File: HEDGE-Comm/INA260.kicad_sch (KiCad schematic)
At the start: 4 parts, among them U6 INA260

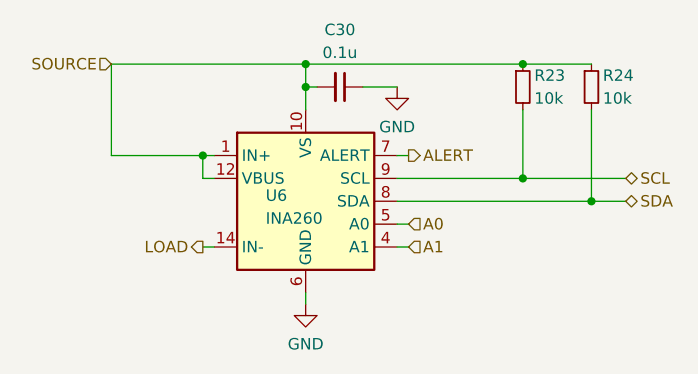
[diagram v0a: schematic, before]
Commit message: Refactor Data PCB files; enter RS485; enter Iridium radio power
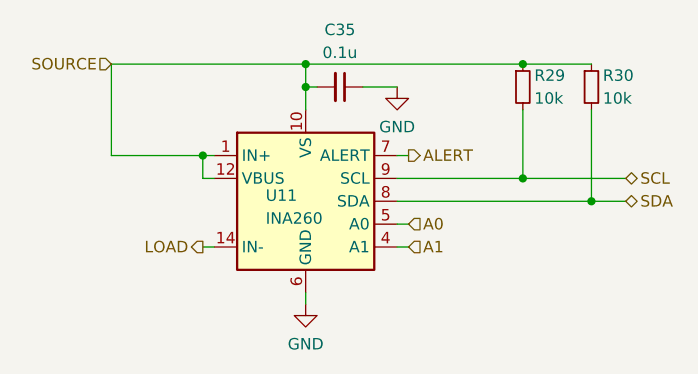
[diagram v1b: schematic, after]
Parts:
- renumbered C30 to C35, R23 to R29, R24 to R30, U6 to U11
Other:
- title: HEDGE-Data PCB -> HEDGE Comm PCB
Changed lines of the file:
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@@
 	(paper "C")
 	(title_block
-		(title "HEDGE-Data PCB")
-		(date "2024-10-09")
+		(title "HEDGE Comm PCB")
+		(date "2024-10-11")
 		(rev "1.0")
 		(company "Spacecraft Design Lab")
@@
 		(on_board yes)
 		(dnp no)
-		(property "Reference" "U6"
+		(property "Reference" "U11"
 			(at 276.225 211.455 0)
 			(effects
@@
 		)
 		(instances
-			(project "HEDGE-Data"
-				(path "/02a0bd66-ef06-41e3-be4b-cca89913b2e5/239e3f0e-d101-4327-8c6c-1d7f43f9fa83"
-					(reference "U6")
-					(unit 1)
-				)
-				(path "/02a0bd66-ef06-41e3-be4b-cca89913b2e5/3d8b74a1-ff69-40df-90d3-fa5176499046"
-					(reference "U7")
-					(unit 1)
-				)
-				(path "/02a0bd66-ef06-41e3-be4b-cca89913b2e5/40d2e298-2505-4869-b40b-0e03f2c17fb7"
-					(reference "U8")
+			(project "Comm"
+				(path "/02a0bd66-ef06-41e3-be4b-cca89913b2e5/98516715-195b-4218-bcff-d5194ed70cb8"
+					(reference "U11")
 					(unit 1)
 				)
@@
 		(dnp no)
 		(fields_autoplaced yes)
-		(property "Reference" "C30"
+		(property "Reference" "C35"
 			(at 284.4736 193.04 90)
 			(effects
@@
 		)
 		(instances
-			(project "HEDGE-Data"
-				(path "/02a0bd66-ef06-41e3-be4b-cca89913b2e5/239e3f0e-d101-4327-8c6c-1d7f43f9fa83"
-					(reference "C30")
-					(unit 1)
-				)
-				(path "/02a0bd66-ef06-41e3-be4b-cca89913b2e5/3d8b74a1-ff69-40df-90d3-fa5176499046"
-					(reference "C31")
-					(unit 1)
-				)
-				(path "/02a0bd66-ef06-41e3-be4b-cca89913b2e5/40d2e298-2505-4869-b40b-0e03f2c17fb7"
-					(reference "C32")
+			(project "Comm"
+				(path "/02a0bd66-ef06-41e3-be4b-cca89913b2e5/98516715-195b-4218-bcff-d5194ed70cb8"
+					(reference "C35")
 					(unit 1)
 				)
@@
 		(on_board yes)
 		(dnp no)
-		(property "Reference" "R24"
+		(property "Reference" "R30"
 			(at 313.69 198.12 0)
 			(effects
@@
 		)
 		(instances
-			(project "HEDGE-Data"
-				(path "/02a0bd66-ef06-41e3-be4b-cca89913b2e5/239e3f0e-d101-4327-8c6c-1d7f43f9fa83"
-					(reference "R24")
-					(unit 1)
-				)
-				(path "/02a0bd66-ef06-41e3-be4b-cca89913b2e5/3d8b74a1-ff69-40df-90d3-fa5176499046"
-					(reference "R26")
-					(unit 1)
-				)
-				(path "/02a0bd66-ef06-41e3-be4b-cca89913b2e5/40d2e298-2505-4869-b40b-0e03f2c17fb7"
-					(reference "R28")
+			(project "Comm"
+				(path "/02a0bd66-ef06-41e3-be4b-cca89913b2e5/98516715-195b-4218-bcff-d5194ed70cb8"
+					(reference "R30")
 					(unit 1)
 				)
@@
 		(dnp no)
 		(fields_autoplaced yes)
-		(property "Reference" "#PWR055"
+		(property "Reference" "#PWR067"
 			(at 280.67 229.87 0)
 			(effects
@@
 		)
 		(instances
-			(project "HEDGE-Data"
-				(path "/02a0bd66-ef06-41e3-be4b-cca89913b2e5/239e3f0e-d101-4327-8c6c-1d7f43f9fa83"
-					(reference "#PWR055")
-					(unit 1)
-				)
-				(path "/02a0bd66-ef06-41e3-be4b-cca89913b2e5/3d8b74a1-ff69-40df-90d3-fa5176499046"
-					(reference "#PWR057")
-					(unit 1)
-				)
-				(path "/02a0bd66-ef06-41e3-be4b-cca89913b2e5/40d2e298-2505-4869-b40b-0e03f2c17fb7"
-					(reference "#PWR059")
+			(project "Comm"
+				(path "/02a0bd66-ef06-41e3-be4b-cca89913b2e5/98516715-195b-4218-bcff-d5194ed70cb8"
+					(reference "#PWR067")
 					(unit 1)
 				)
@@
 		(dnp no)
 		(fields_autoplaced yes)
-		(property "Reference" "#PWR056"
+		(property "Reference" "#PWR068"
 			(at 290.83 205.74 0)
 			(effects
@@
 		)
 		(instances
-			(project "HEDGE-Data"
-				(path "/02a0bd66-ef06-41e3-be4b-cca89913b2e5/239e3f0e-d101-4327-8c6c-1d7f43f9fa83"
-					(reference "#PWR056")
-					(unit 1)
-				)
-				(path "/02a0bd66-ef06-41e3-be4b-cca89913b2e5/3d8b74a1-ff69-40df-90d3-fa5176499046"
-					(reference "#PWR058")
-					(unit 1)
-				)
-				(path "/02a0bd66-ef06-41e3-be4b-cca89913b2e5/40d2e298-2505-4869-b40b-0e03f2c17fb7"
-					(reference "#PWR060")
+			(project "Comm"
+				(path "/02a0bd66-ef06-41e3-be4b-cca89913b2e5/98516715-195b-4218-bcff-d5194ed70cb8"
+					(reference "#PWR068")
 					(unit 1)
 				)
@@
 		(on_board yes)
 		(dnp no)
-		(property "Reference" "R23"
+		(property "Reference" "R29"
 			(at 306.07 198.12 0)
 			(effects
@@
 		)
 		(instances
-			(project "HEDGE-Data"
-				(path "/02a0bd66-ef06-41e3-be4b-cca89913b2e5/239e3f0e-d101-4327-8c6c-1d7f43f9fa83"
-					(reference "R23")
+			(project "Comm"
+				(path "/02a0bd66-ef06-41e3-be4b-cca89913b2e5/98516715-195b-4218-bcff-d5194ed70cb8"
+					(reference "R29")
 					(unit 1)
 				)
-				(path "/02a0bd66-ef06-41e3-be4b-cca89913b2e5/3d8b74a1-ff69-40df-90d3-fa5176499046"
-					(reference "R25")
-					(unit 1)
-				)
-				(path "/02a0bd66-ef06-41e3-be4b-cca89913b2e5/40d2e298-2505-4869-b40b-0e03f2c17fb7"
-					(reference "R27")
-					(unit 1)
-				)
